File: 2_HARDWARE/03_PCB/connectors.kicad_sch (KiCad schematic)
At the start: 19 parts, among them J1 TYPE-C-31-M-12, J2 SMA, J3 SMA, J4 BNC, J5 PH-00244

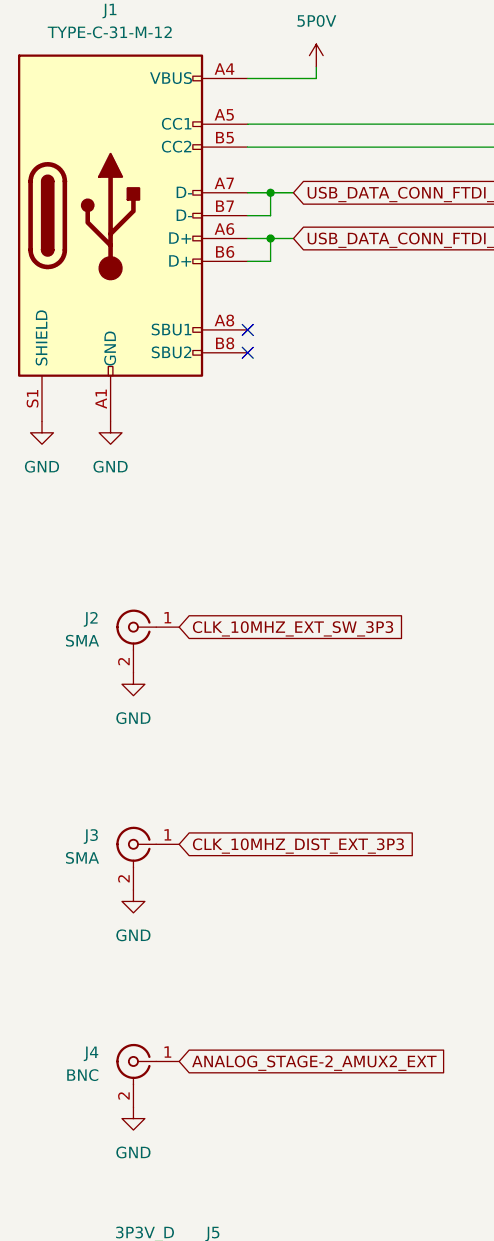
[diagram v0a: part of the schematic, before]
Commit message: MINOR: Adjusted soldermask and ported Schematic + PCB to Kicad 9.0.
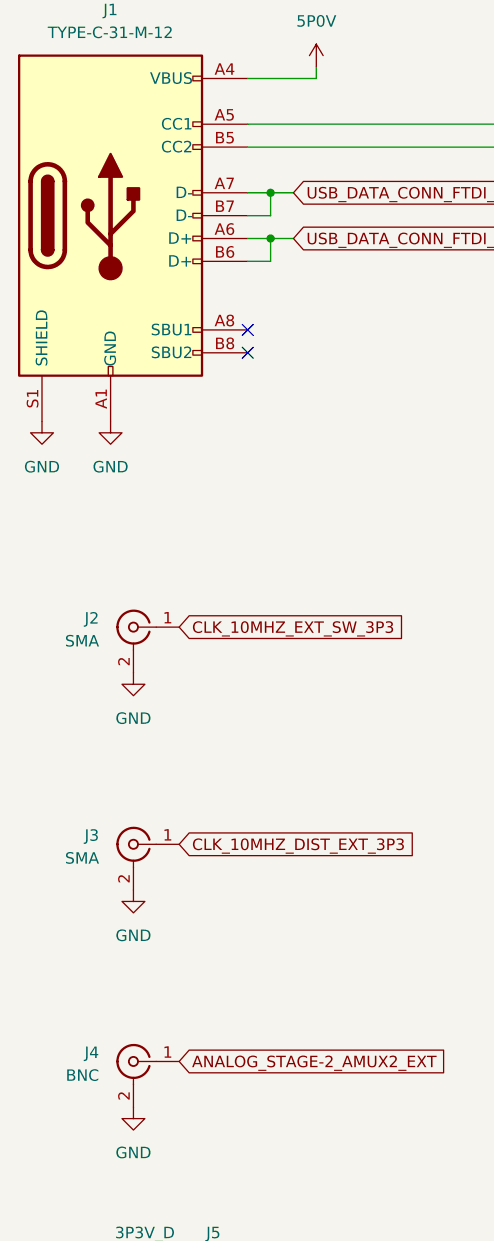
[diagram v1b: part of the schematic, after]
